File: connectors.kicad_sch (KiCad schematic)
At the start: 71 parts

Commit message: Mock placement of all components on schematic
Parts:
- removed D? (x9): LED_G_0603_LG_L29K-G2J1-24-Z, antmicro-footprints:LED_0603_1608Metric_G, symbol antmicroLEDIndicationDiscrete:LED_G_0603_LG_L29K-G2J1-24-Z
- removed J? (x8): Conn_1-2212115-4, antmicro-footprints:Conn_1-2212115-4, symbol antmicroB2bConnectors:Conn_1-2212115-4
- removed R? (x8): R_4k7_0603, antmicro-footprints:R_0603_1608Metric, symbol antmicroResistors0603:R_4k7_0603
- removed R?: R_2k2_0603, antmicro-footprints:R_0603_1608Metric, symbol antmicroResistors0603:R_2k2_0603
- added R? (x2): R_0R_0805, antmicro-footprints:R_0805_2012Metric, symbol antmicroResistorsmisc:R_0R_0805
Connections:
- net VCC12V0: now also R?.1
- net 12V_ALWAYS_ON: now reaches J?.P19/20
- net 12V_ALWAYS_ON: now also R?.1
- new net 12V_INTERNAL: R?.2, R?.2
- no-connect marks 9 -> 8
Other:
- note removed: "Power Indicators"
- note removed: "thunderbolt-gpu-adapter connectors"
- moved on the sheet: C?, D?, FB?, J?, Q?, R?, S?, TP?, U?

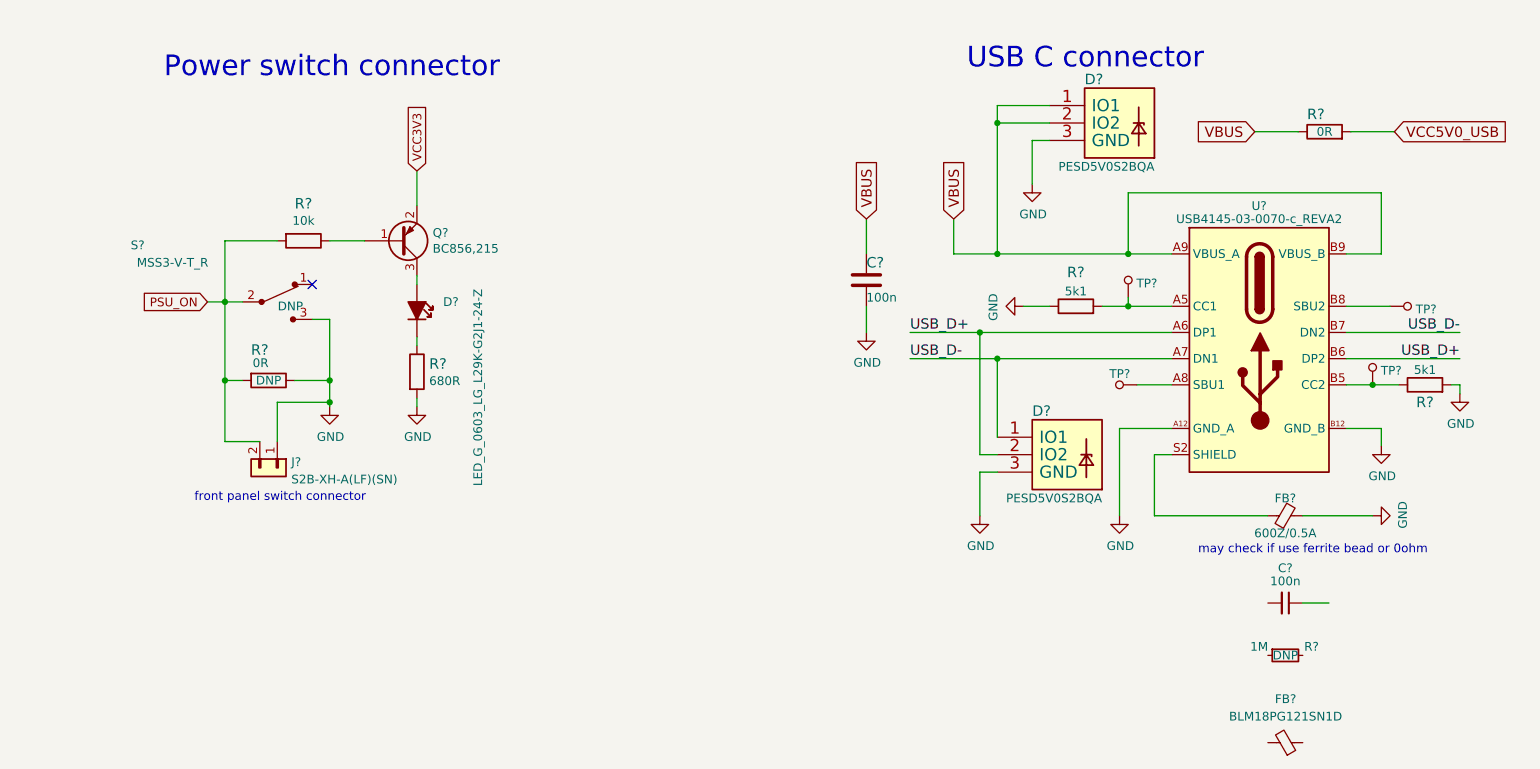
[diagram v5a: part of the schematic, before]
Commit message: Rearrange pwr flags
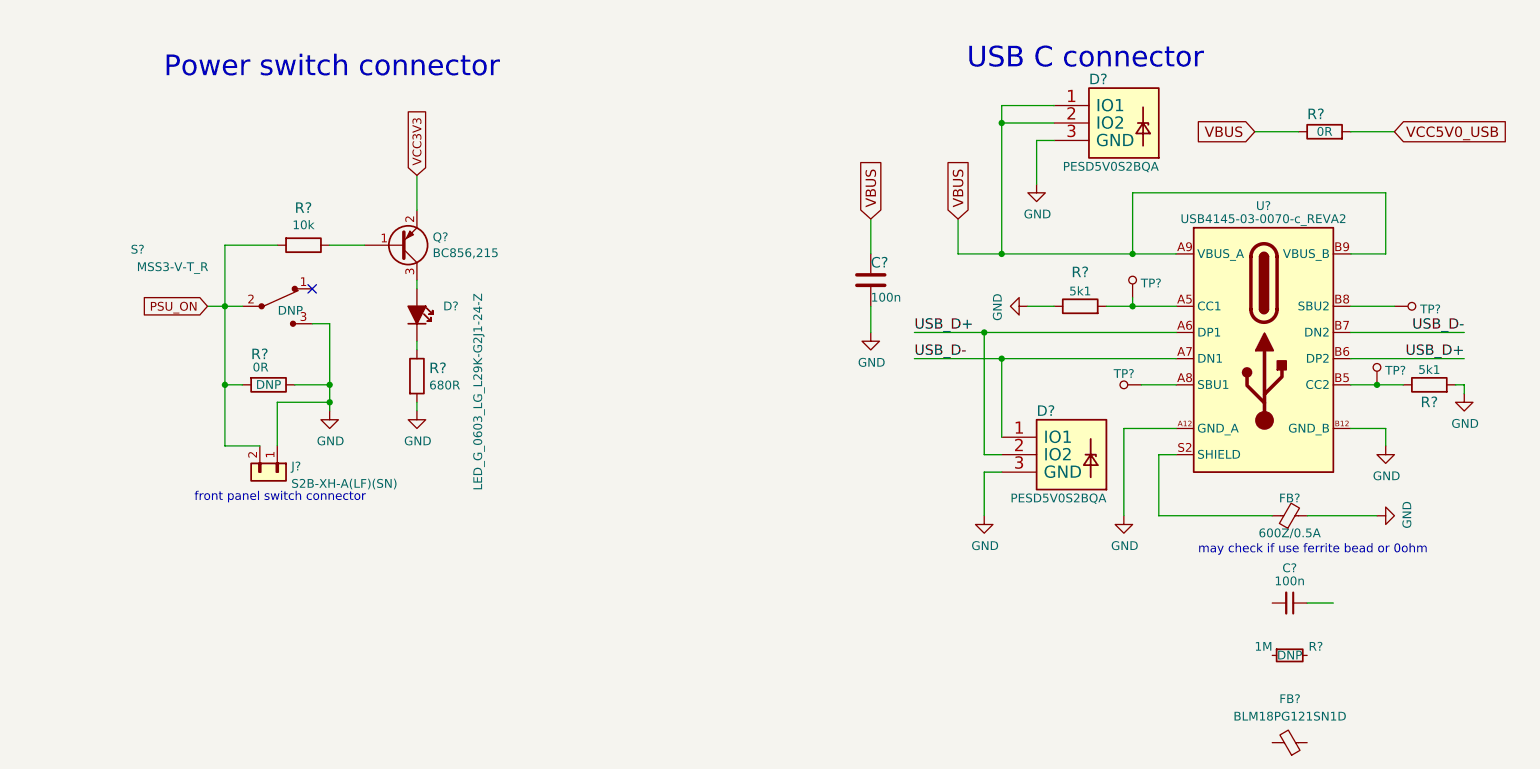
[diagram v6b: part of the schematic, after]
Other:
- moved on the sheet: C?, D?, FB?, J?, Q?, R?, S?, TP?, U?

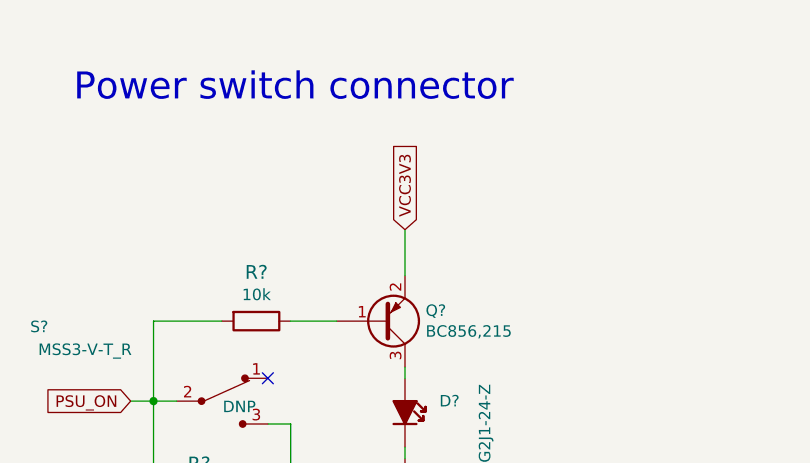
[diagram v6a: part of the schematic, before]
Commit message: Change power flags on schematic
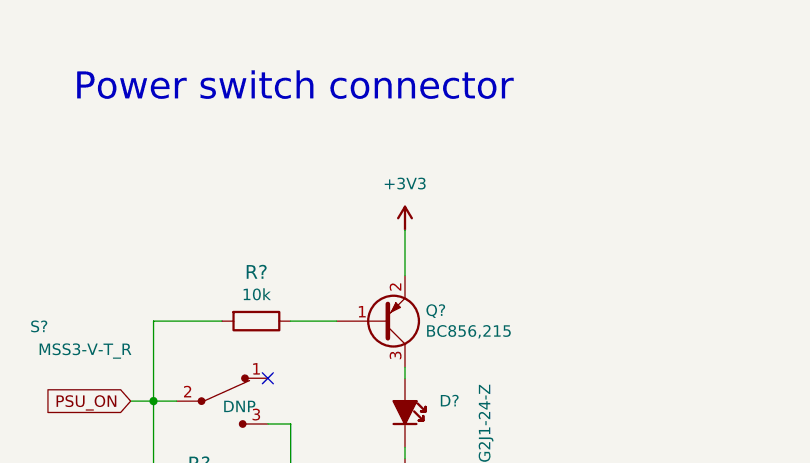
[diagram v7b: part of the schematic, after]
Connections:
- net VCC3V3 renamed +3V3
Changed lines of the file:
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@@
-    )
-  )
-  (global_label "VCC3V3" (shape input) (at 218.44 113.03 90) (fields_autoplaced)
-    (effects (font (size 1.27 1.27)) (justify left))
-    (property "Intersheet References" "${INTERSHEET_REFS}" (id 0) (at 60.96 88.265 0)
-      (effects (font (size 1.27 1.27)) hide)
     )
   )
@@
     )
     (pin "1")
+  )
+  (symbol (lib_id "antmicropower:+3V3") (at 218.44 113.03 0) (unit 1)
+    (in_bom yes) (on_board yes) (fields_autoplaced)
+    (property "Reference" "#PWR?" (id 0) (at 233.68 115.57 0)
+      (effects (font (size 1.27 1.27) (thickness 0.15)) (justify left bottom) hide)
+    )
+    (property "Value" "+3V3" (id 1) (at 218.44 107.95 0)
+      (effects (font (size 1.27 1.27) (thickness 0.15)))
+    )
+    (property "Footprint" "" (id 2) (at 233.68 120.65 0)
+      (effects (font (size 1.27 1.27) (thickness 0.15)) (justify left bottom) hide)
+    )
+    (property "Datasheet" "" (id 3) (at 233.68 123.19 0)
+      (effects (font (size 1.27 1.27) (thickness 0.15)) (justify left bottom) hide)
+    )
+    (property "Author" "Antmicro" (id 4) (at 233.68 120.65 0)
+      (effects (font (size 1.27 1.27) (thickness 0.15)) (justify left bottom) hide)
+    )
+    (property "License" "Apache-2.0" (id 5) (at 233.68 123.19 0)
+      (effects (font (size 1.27 1.27) (thickness 0.15)) (justify left bottom) hide)
+    )
+    (pin "1")

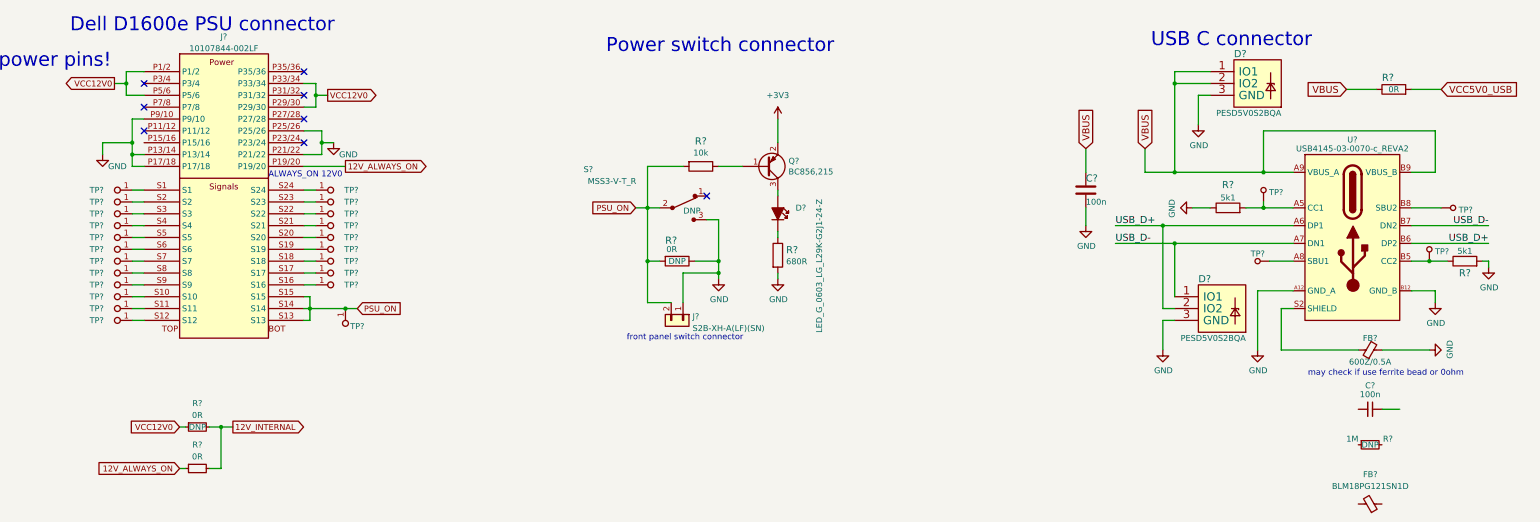
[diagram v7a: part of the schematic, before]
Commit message: Reannotate schematic symbols
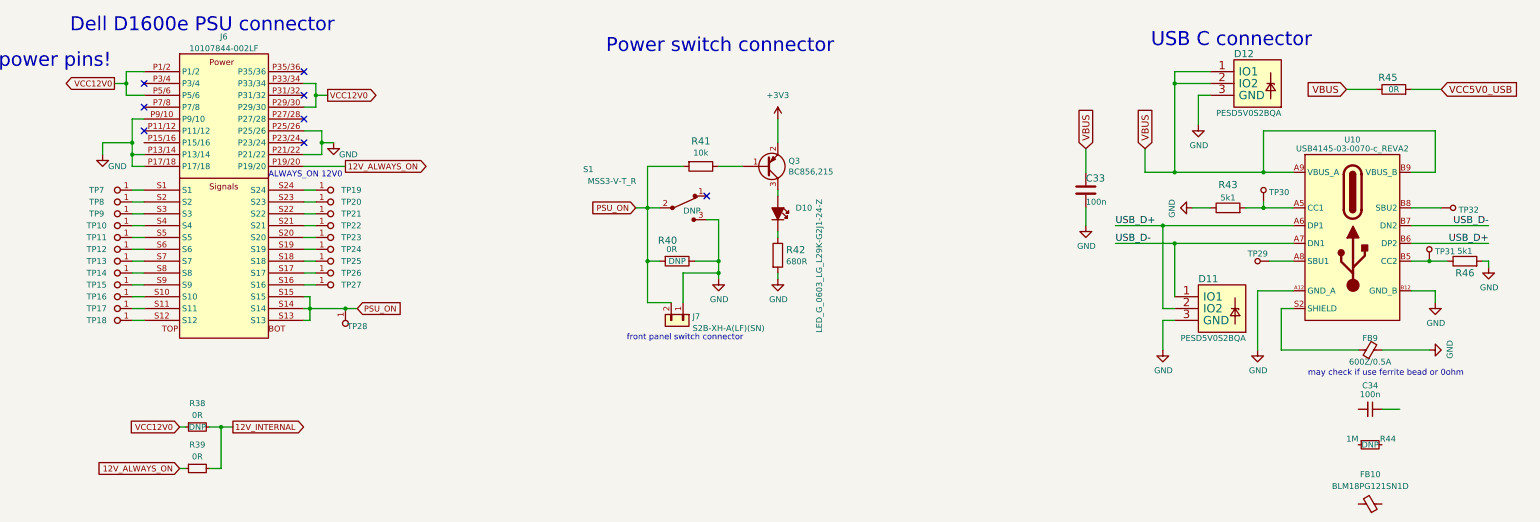
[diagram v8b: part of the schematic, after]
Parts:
- gave numbers to parts that had none: 47
